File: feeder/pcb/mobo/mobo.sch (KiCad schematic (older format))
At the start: 64 parts, among them J1 FTDI_HEADER, J2 PLATED_PADS, J3 SWD_10, M1 DRIVE_MOTOR, M2 PEEL_MOTOR, SW1 BUTTON_1, SW2 BUTTON_2, SW3 RESET, U1 TCS40DPR, U2 VCNT2020, U3 MAX3485, U4 DRV8833PWP, U5 AP1117-33, U6 STM32F103C8Tx, U7 MCP16301, U8 QRE1113, Y1 8MHz

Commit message: Changed RS-485 transciever to MAX3078E
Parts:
- removed U3: MAX3485, Package_SO:SOIC-8_3.9x4.9mm_P1.27mm, symbol Interface_UART:MAX3485
- added U3: MAX3078E, Package_SO:SOIC-8_3.9x4.9mm_P1.27mm, symbol Interface_UART:MAX3078E
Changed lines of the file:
@@
 L power:GND #PWR0103
 U 1 1 5F5FF902
-P 10250 4850
-F 0 "#PWR0103" H 10250 4600 50  0001 C CNN
-F 1 "GND" H 10255 4677 50  0000 C CNN
-F 2 "" H 10250 4850 50  0001 C CNN
-F 3 "" H 10250 4850 50  0001 C CNN
-	1    10250 4850
+P 10250 4725
+F 0 "#PWR0103" H 10250 4475 50  0001 C CNN
+F 1 "GND" H 10255 4552 50  0000 C CNN
+F 2 "" H 10250 4725 50  0001 C CNN
+F 3 "" H 10250 4725 50  0001 C CNN
+	1    10250 4725
 	1    0    0    -1
 $EndComp
@@
 	1    0    0    -1
 $EndComp
-Text GLabel 10650 4150 2    50   Input ~ 0
-RS-485-
 $Comp
 L Device:C_Small C6
@@
 	1    0    0    -1
 $EndComp
-Text GLabel 10650 4450 2    50   Input ~ 0
-RS-485+
 $Comp
 L Device:C_Small C2
@@
 Text GLabel 3875 6800 2    50   Input ~ 0
 FILM_TENSION
-Text GLabel 9700 4450 0    50   Input ~ 0
-MCU_TX
-Text GLabel 9550 4350 0    50   Input ~ 0
-DE
-Text GLabel 9700 4150 0    50   Input ~ 0
+Text GLabel 9700 4125 0    50   Input ~ 0
 MCU_RX
 $Comp
 L power:+3V3 #PWR0128
 U 1 1 5F6C97D4
-P 10250 3750
-F 0 "#PWR0128" H 10250 3600 50  0001 C CNN
-F 1 "+3V3" H 10265 3923 50  0000 C CNN
-F 2 "" H 10250 3750 50  0001 C CNN
-F 3 "" H 10250 3750 50  0001 C CNN
-	1    10250 3750
+P 10250 3925
+F 0 "#PWR0128" H 10250 3775 50  0001 C CNN
+F 1 "+3V3" H 10265 4098 50  0000 C CNN
+F 2 "" H 10250 3925 50  0001 C CNN
+F 3 "" H 10250 3925 50  0001 C CNN
+	1    10250 3925
 	1    0    0    -1
 $EndComp
@@
 	1    0    0    -1
 $EndComp
-$Comp
-L Interface_UART:MAX3485 U3
-U 1 1 5F624AB7
-P 10250 4250
-F 0 "U3" H 10050 4600 50  0000 C CNN
-F 1 "MAX3485" H 10450 4700 50  0000 C CNN
-F 2 "Package_SO:SOIC-8_3.9x4.9mm_P1.27mm" H 10250 3550 50  0001 C CNN
-F 3 "https://datasheets.maximintegrated.com/en/ds/MAX3483-MAX3491.pdf" H 10250 4300 50  0001 C CNN
-F 4 "C40031" H 10250 4250 50  0001 C CNN "JLCPCB"
-	1    10250 4250
-	1    0    0    -1
-$EndComp
-Wire Wire Line
-	9700 4150 9850 4150
-Wire Wire Line
-	9700 4450 9850 4450
+Wire Wire Line
+	9700 4125 9850 4125
 Wire Wire Line
 	6600 5350 6800 5350
@@
 Text GLabel 2750 2350 0    50   Input ~ 0
 LED5
-Text GLabel 9550 4250 0    50   Input ~ 0
+Text GLabel 9550 4225 0    50   Input ~ 0
 _RE
 Wire Wire Line
-	9550 4250 9850 4250
-Wire Wire Line
-	9550 4350 9850 4350
+	9550 4225 9850 4225
 Text GLabel 4050 3350 2    50   Input ~ 0
 _RE
@@
 $EndComp
 Connection ~ 8975 1275
+$Comp
+L Interface_UART:MAX3078E U3
+U 1 1 602E6D5D
+P 10250 4325
+F 0 "U3" H 10375 4800 50  0000 C CNN
+F 1 "MAX3078E" H 10500 4700 50  0000 C CNN
+F 2 "Package_SO:SOIC-8_3.9x4.9mm_P1.27mm" H 11300 3975 50  0001 C CIN
+F 3 "https://datasheets.maximintegrated.com/en/ds/MAX3070E-MAX3079E.pdf" H 10250 4325 50  0001 C CNN
+F 4 "C40031" H 10250 4325 50  0001 C CNN "JLCPCB"
+F 5 "C40031" H 10250 4325 50  0001 C CNN "LCSC"
+	1    10250 4325
+	1    0    0    -1
+$EndComp
+Text GLabel 10650 4425 2    50   Input ~ 0
+RS-485-
+Text GLabel 10650 4225 2    50   Input ~ 0
+RS-485+
+Wire Wire Line
+	9700 4525 9850 4525
+Text GLabel 9700 4525 0    50   Input ~ 0
+MCU_TX
+Wire Wire Line
+	9550 4425 9850 4425
+Text GLabel 9550 4425 0    50   Input ~ 0
+DE
 $EndSCHEMATC

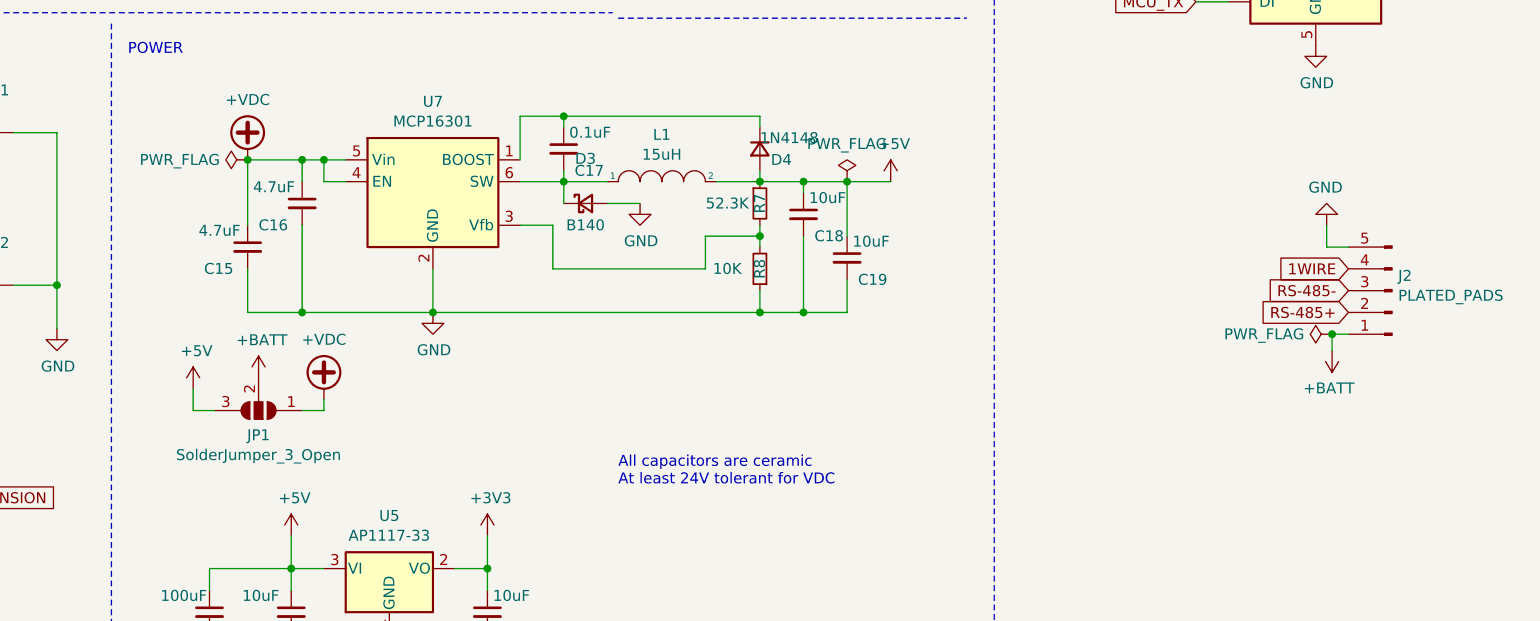
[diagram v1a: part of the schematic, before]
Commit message: removed power jumer in schematic, fixed SWD footprint
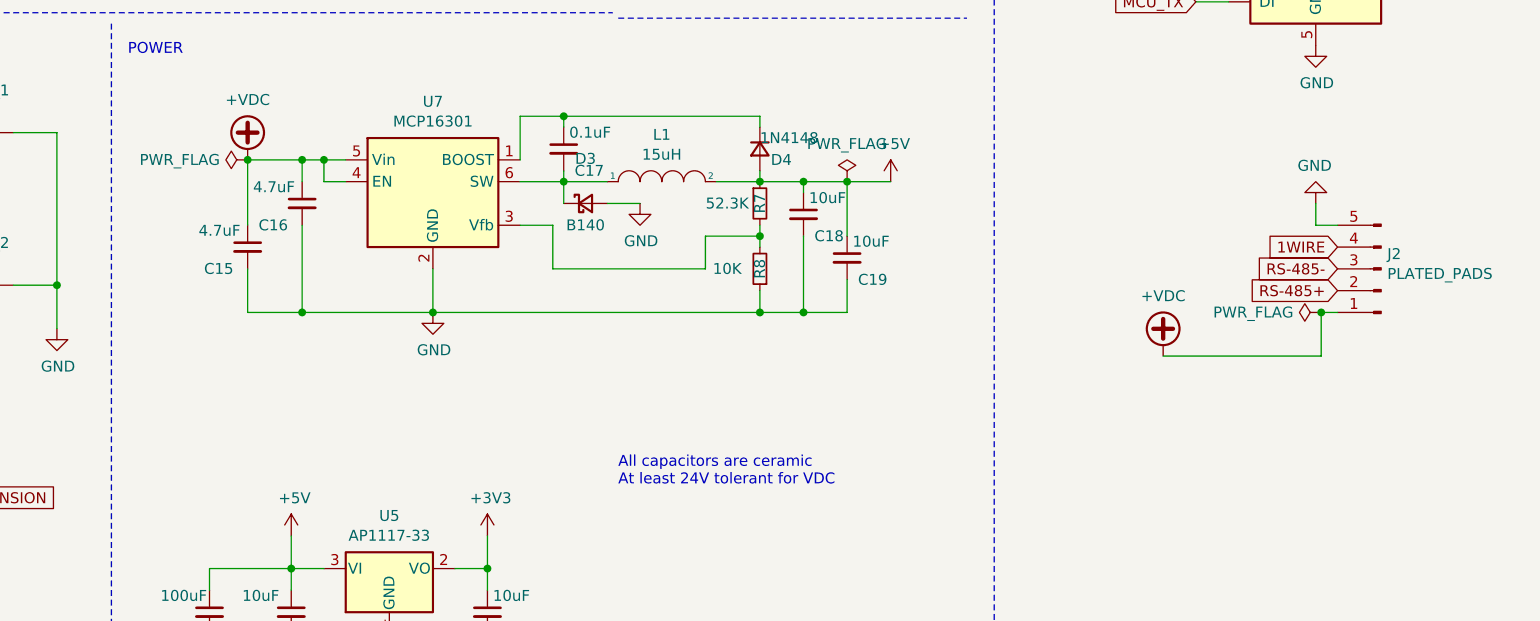
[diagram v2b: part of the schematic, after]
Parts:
- removed JP1: SolderJumper_3_Open, Jumper:SolderJumper-3_P1.3mm_Open_RoundedPad1.0x1.5mm, symbol Jumper:SolderJumper_3_Open
- J3: footprint Connector_PinHeader_1.00mm:PinHeader_2x05_P1.00mm_Vertical_SMD -> Connector_PinHeader_1.27mm:PinHeader_2x05_P1.27mm_Vertical_SMD
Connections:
- net +BATT is gone; now on net +VDC: J2.1 (Pin_1)
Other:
- moved on the sheet: J2
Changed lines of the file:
@@
 L power:GND #PWR0102
 U 1 1 5DC9F0F0
-P 10300 5550
-F 0 "#PWR0102" H 10300 5300 50  0001 C CNN
-F 1 "GND" H 10305 5377 50  0000 C CNN
-F 2 "" H 10300 5550 50  0001 C CNN
-F 3 "" H 10300 5550 50  0001 C CNN
-	1    10300 5550
+P 10250 5450
+F 0 "#PWR0102" H 10250 5200 50  0001 C CNN
+F 1 "GND" H 10255 5277 50  0000 C CNN
+F 2 "" H 10250 5450 50  0001 C CNN
+F 3 "" H 10250 5450 50  0001 C CNN
+	1    10250 5450
 	-1   0    0    1
 $EndComp
@@
 F 0 "J3" H 925 3875 50  0000 R CNN
 F 1 "SWD_10" H 1575 2775 50  0000 R CNN
-F 2 "Connector_PinHeader_1.00mm:PinHeader_2x05_P1.00mm_Vertical_SMD" H 1225 3325 50  0001 C CNN
+F 2 "Connector_PinHeader_1.27mm:PinHeader_2x05_P1.27mm_Vertical_SMD" H 1225 3325 50  0001 C CNN
 F 3 "http://infocenter.arm.com/help/topic/com.arm.doc.ddi0314h/DDI0314H_coresight_components_trm.pdf" V 875 2075 50  0001 C CNN
 	1    1225 3325
@@
 	3550 825  3650 825
 Wire Wire Line
-	10325 6125 10325 6050
-Wire Wire Line
-	10325 6050 10400 6050
+	10275 5950 10350 5950
 $Comp
 L Connector:Conn_01x05_Male J2
 U 1 1 5FEEFFA2
-P 10600 5850
-F 0 "J2" H 10572 5782 50  0000 R CNN
-F 1 "PLATED_PADS" H 10572 5873 50  0000 R CNN
-F 2 "index:5-pad-spring-finger-interface" H 10600 5850 50  0001 C CNN
-F 3 "~" H 10600 5850 50  0001 C CNN
-	1    10600 5850
+P 10550 5750
+F 0 "J2" H 10522 5682 50  0000 R CNN
+F 1 "PLATED_PADS" H 10522 5773 50  0000 R CNN
+F 2 "index:5-pad-spring-finger-interface" H 10550 5750 50  0001 C CNN
+F 3 "~" H 10550 5750 50  0001 C CNN
+	1    10550 5750
 	-1   0    0    1
 $EndComp
@@
 	7700 5350 7700 5300
 $Comp
-L Jumper:SolderJumper_3_Open JP1
-U 1 1 602D5546
-P 5400 6400
-F 0 "JP1" H 5400 6513 50  0000 C CNN
-F 1 "SolderJumper_3_Open" H 5400 6604 50  0000 C CNN
-F 2 "Jumper:SolderJumper-3_P1.3mm_Open_RoundedPad1.0x1.5mm" H 5400 6400 50  0001 C CNN
-F 3 "~" H 5400 6400 50  0001 C CNN
-	1    5400 6400
-	-1   0    0    1
-$EndComp
-$Comp
 L power:+VDC #PWR0138
 U 1 1 602D9299
-P 5700 6350
-F 0 "#PWR0138" H 5700 6250 50  0001 C CNN
-F 1 "+VDC" H 5700 6625 50  0000 C CNN
-F 2 "" H 5700 6350 50  0001 C CNN
-F 3 "" H 5700 6350 50  0001 C CNN
-	1    5700 6350
-	1    0    0    -1
-$EndComp
-$Comp
-L power:+BATT #PWR0139
-U 1 1 602DA2B0
-P 10325 6125
-F 0 "#PWR0139" H 10325 5975 50  0001 C CNN
-F 1 "+BATT" H 10340 6298 50  0000 C CNN
-F 2 "" H 10325 6125 50  0001 C CNN
-F 3 "" H 10325 6125 50  0001 C CNN
-	1    10325 6125
-	-1   0    0    1
-$EndComp
-Wire Wire Line
-	10300 5550 10300 5650
-Wire Wire Line
-	10300 5650 10400 5650
-$Comp
-L power:+BATT #PWR0140
-U 1 1 603001A0
-P 5400 6250
-F 0 "#PWR0140" H 5400 6100 50  0001 C CNN
-F 1 "+BATT" H 5415 6423 50  0000 C CNN
-F 2 "" H 5400 6250 50  0001 C CNN
-F 3 "" H 5400 6250 50  0001 C CNN
-	1    5400 6250
-	1    0    0    -1
-$EndComp
-Wire Wire Line
-	5600 6400 5700 6400
-Wire Wire Line
-	5700 6400 5700 6350
-$Comp
-L power:+5V #PWR0141
-U 1 1 60312EB9
-P 5100 6300
-F 0 "#PWR0141" H 5100 6150 50  0001 C CNN
-F 1 "+5V" H 5115 6473 50  0000 C CNN
-F 2 "" H 5100 6300 50  0001 C CNN
-F 3 "" H 5100 6300 50  0001 C CNN
-	1    5100 6300
-	1    0    0    -1
-$EndComp
-Wire Wire Line
-	5100 6300 5100 6400
-Wire Wire Line
-	5100 6400 5200 6400
+P 9550 6150
+F 0 "#PWR0138" H 9550 6050 50  0001 C CNN
+F 1 "+VDC" H 9550 6425 50  0000 C CNN
+F 2 "" H 9550 6150 50  0001 C CNN
+F 3 "" H 9550 6150 50  0001 C CNN
+	1    9550 6150
+	1    0    0    -1
+$EndComp
+Wire Wire Line
+	10250 5450 10250 5550
+Wire Wire Line
+	10250 5550 10350 5550
 $Comp
 L index:TCS40DPR U1
@@
 Wire Wire Line
 	7650 3975 7650 4075
-Text GLabel 10400 5750 0    50   Input ~ 0
+Text GLabel 10350 5650 0    50   Input ~ 0
 1WIRE
-Text GLabel 10400 5850 0    50   Input ~ 0
+Text GLabel 10350 5750 0    50   Input ~ 0
 RS-485-
-Text GLabel 10400 5950 0    50   Input ~ 0
+Text GLabel 10350 5850 0    50   Input ~ 0
 RS-485+
 Text GLabel 2100 5750 0    50   Input ~ 0
@@
 L power:PWR_FLAG #FLG0102
 U 1 1 601DEE7F
-P 10325 6050
-F 0 "#FLG0102" H 10325 6125 50  0001 C CNN
-F 1 "PWR_FLAG" V 10325 6177 50  0000 L CNN
-F 2 "" H 10325 6050 50  0001 C CNN
-F 3 "~" H 10325 6050 50  0001 C CNN
-	1    10325 6050
+P 10275 5950
+F 0 "#FLG0102" H 10275 6025 50  0001 C CNN
+F 1 "PWR_FLAG" V 10275 6077 50  0000 L CNN
+F 2 "" H 10275 5950 50  0001 C CNN
+F 3 "~" H 10275 5950 50  0001 C CNN
+	1    10275 5950
 	0    -1   -1   0
 $EndComp
-Connection ~ 10325 6050
+Connection ~ 10275 5950
 NoConn ~ 2750 2550
 NoConn ~ 2750 2650
@@
 Text GLabel 9550 4425 0    50   Input ~ 0
 DE
+Wire Wire Line
+	9550 6150 10275 6150
+Wire Wire Line
+	10275 5950 10275 6150
 $EndSCHEMATC

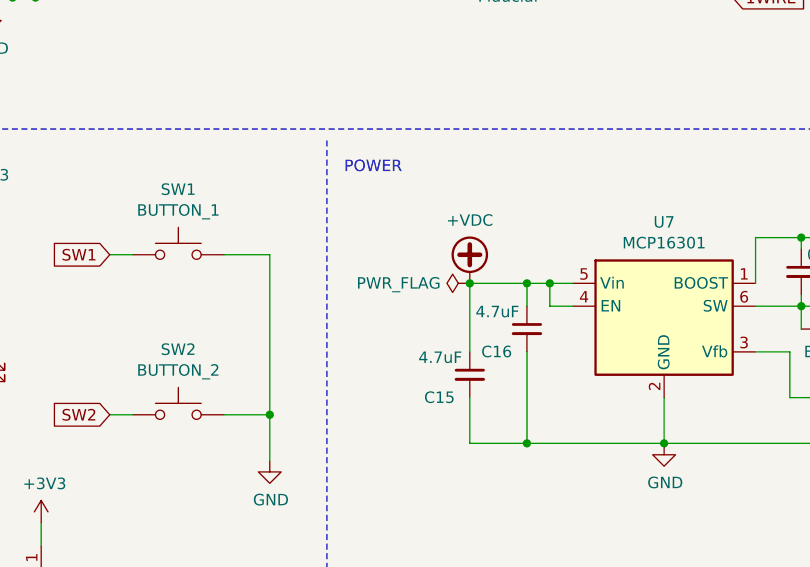
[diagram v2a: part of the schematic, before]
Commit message: Updates to add the KiBot variants for the optical sensor.
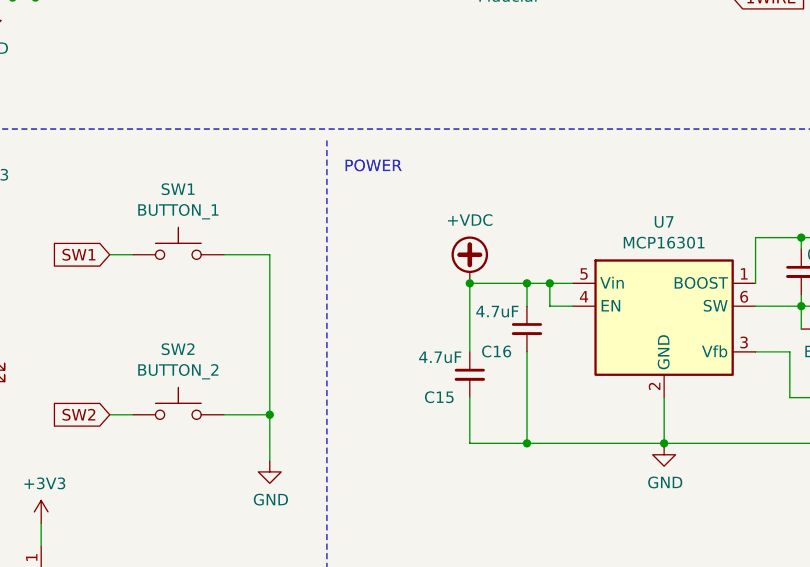
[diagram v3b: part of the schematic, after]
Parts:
- R14, R15, U2: Config (none) -> +VCNT2020
- R5, R6, U8: Config (none) -> -VCNT2020
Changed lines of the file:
@@
 F 3 "~" H 1000 6450 50  0001 C CNN
 F 4 "C17710" H 1000 6450 50  0001 C CNN "JLCPCB"
+F 5 "-VCNT2020" H 1000 6450 50  0001 C CNN "Config"
 	1    1000 6450
 	0    -1   -1   0
@@
 F 3 "~" H 2050 6300 50  0001 C CNN
 F 4 "C17414" H 2050 6300 50  0001 C CNN "JLCPCB"
+F 5 "-VCNT2020" H 2050 6300 50  0001 C CNN "Config"
 	1    2050 6300
 	-1   0    0    1
@@
 	1    0    0    -1
 $EndComp
-Wire Wire Line
-	5350 5250 5600 5250
 Connection ~ 5700 5250
 Wire Wire Line
@@
 F 3 "http://www.onsemi.com/pub/Collateral/QRE1113-D.PDF" H 1550 6650 50  0001 C CNN
 F 4 "C232862" H 1550 6550 50  0001 C CNN "JLCPCB"
+F 5 "-VCNT2020" H 1550 6550 50  0001 C CNN "Config"
 	1    1550 6550
 	1    0    0    -1
@@
 F 2 "index:VCNT2020" H 1250 7550 50  0001 C CNN
 F 3 "" H 1250 7550 50  0001 C CNN
+F 4 "+VCNT2020" H 1250 7550 50  0001 C CNN "Config"
+F 5 "" H 1250 7550 50  0001 C CNN "JLCPCB"
 	1    1250 7550
 	1    0    0    -1
@@
 F 3 "~" H 1000 7200 50  0001 C CNN
 F 4 "C17710" H 1000 7200 50  0001 C CNN "JLCPCB"
+F 5 "+VCNT2020" H 1000 7200 50  0001 C CNN "Config"
 	1    1000 7200
 	0    -1   -1   0
@@
 F 3 "~" H 2200 7400 50  0001 C CNN
 F 4 "C17414" H 2200 7400 50  0001 C CNN "JLCPCB"
+F 5 "+VCNT2020" H 2200 7400 50  0001 C CNN "Config"
 	1    2200 7400
 	0    -1   -1   0
@@
 NoConn ~ 2750 2750
 $Comp
-L power:PWR_FLAG #FLG0103
-U 1 1 602181DE
-P 5350 5250
-F 0 "#FLG0103" H 5350 5325 50  0001 C CNN
-F 1 "PWR_FLAG" V 5350 5377 50  0000 L CNN
-F 2 "" H 5350 5250 50  0001 C CNN
-F 3 "~" H 5350 5250 50  0001 C CNN
-	1    5350 5250
-	0    -1   -1   0
-$EndComp
-$Comp
 L power:PWR_FLAG #FLG0104
 U 1 1 6021C14B
@@
 Wire Wire Line
 	10275 5950 10275 6150
+Wire Wire Line
+	5350 5250 5600 5250
 $EndSCHEMATC

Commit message: Add LCSC Crystal PN
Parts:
- Y1: LCSC (none) -> C518155
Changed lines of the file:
@@
 F 3 "~" H 1950 1650 50  0001 C CNN
 F 4 "C57131" H 1950 1650 50  0001 C CNN "JLCPCB"
+F 5 "C518155" H 1950 1650 50  0001 C CNN "LCSC"
 	1    1950 1650
 	1    0    0    -1
